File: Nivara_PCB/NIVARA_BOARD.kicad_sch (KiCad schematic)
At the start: 3 parts, among them U1 ESP32-S3-WROOM-1

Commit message: Cambios en la power supply.
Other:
- moved on the sheet: C1, R1, U1

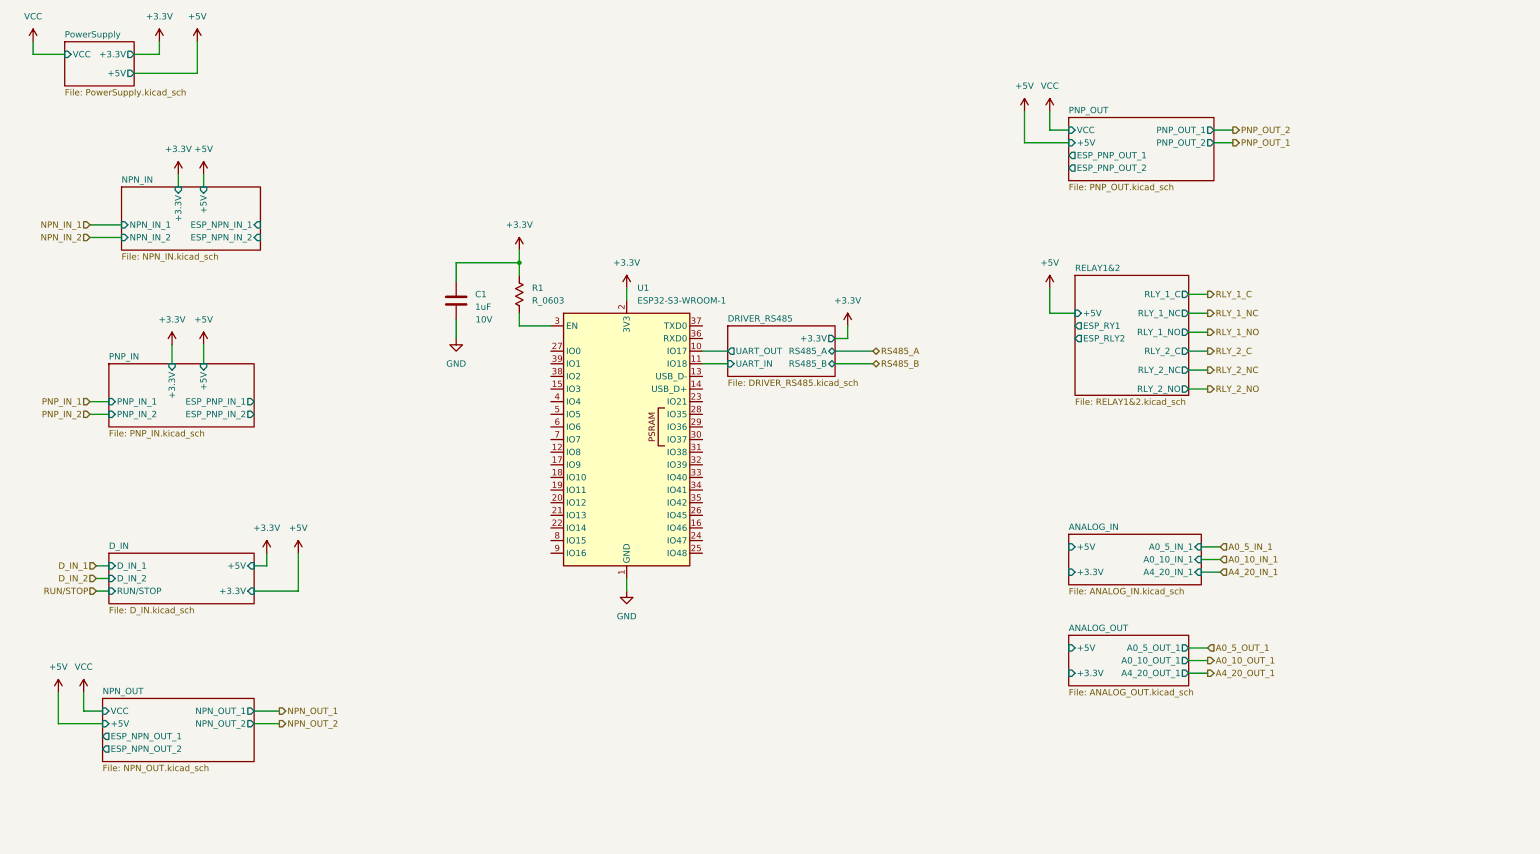
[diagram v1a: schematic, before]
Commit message: Cambios en las mediciones análogas.
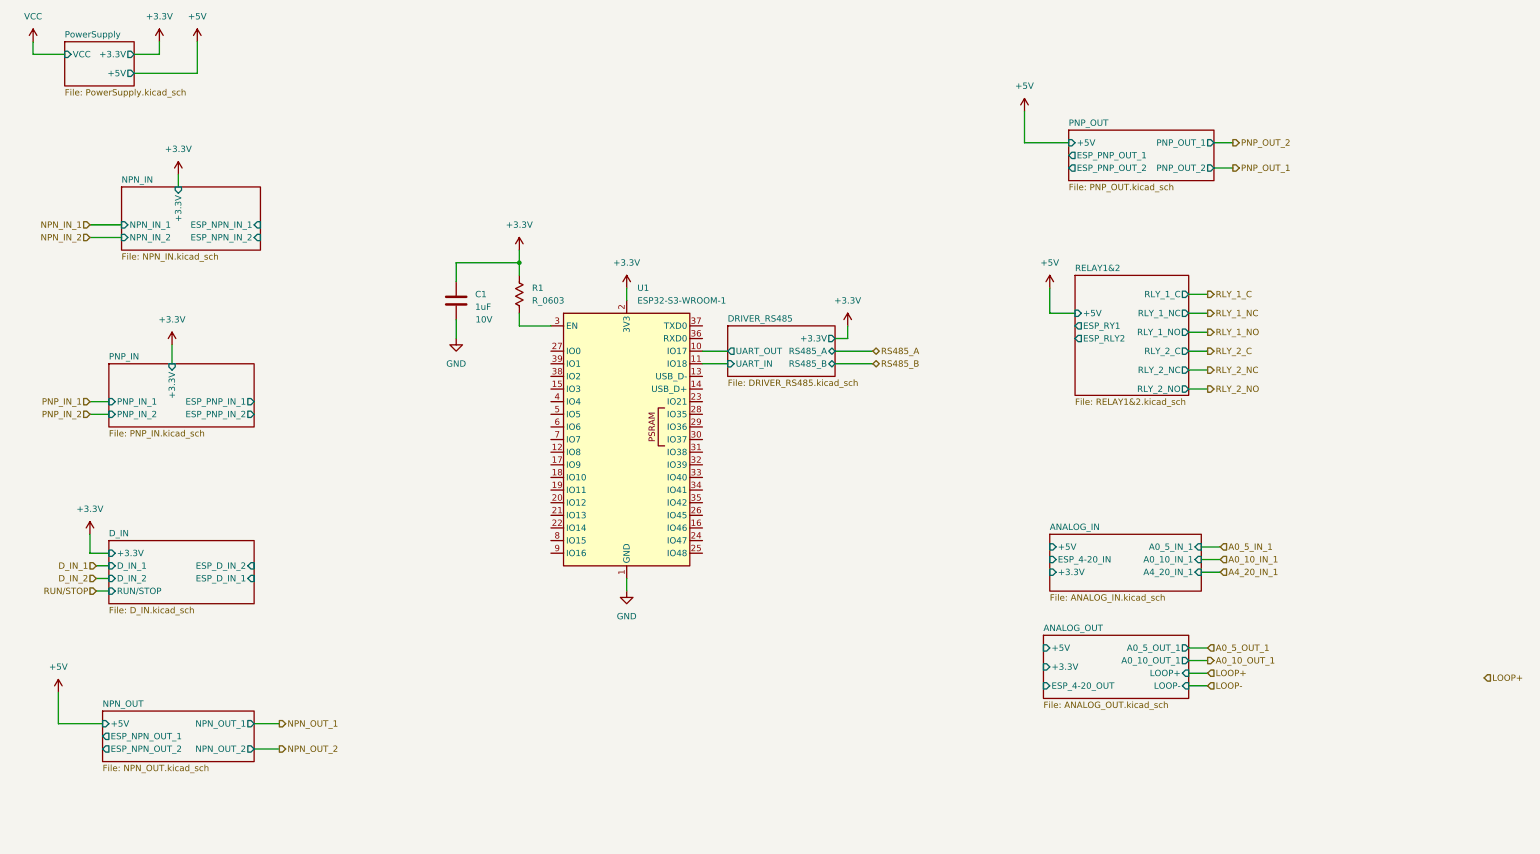
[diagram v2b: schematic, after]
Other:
- sheet ANALOG_IN ports: added ESP_4-20_IN; removed none
- sheet ANALOG_OUT ports: added ESP_4-20_OUT, LOOP+, LOOP-; removed A4_20_OUT_1
- sheet D_IN ports: added ESP_D_IN_1, ESP_D_IN_2; removed +5V
- sheet NPN_IN ports: added none; removed +5V
- sheet NPN_OUT ports: added none; removed VCC
- sheet PNP_IN ports: added none; removed +5V
- sheet PNP_OUT ports: added none; removed VCC

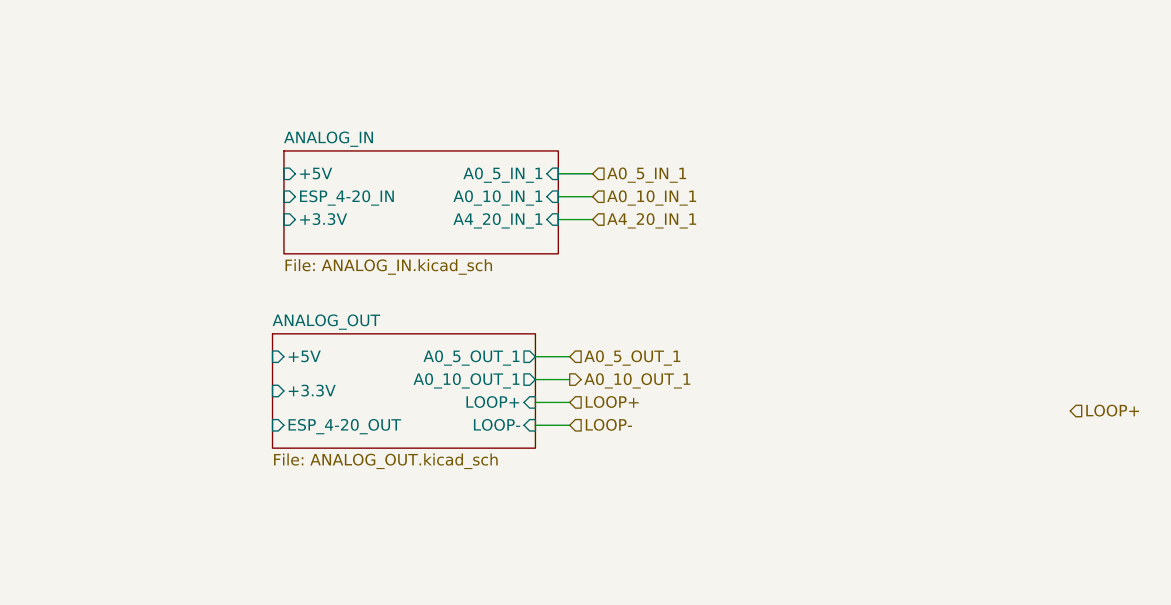
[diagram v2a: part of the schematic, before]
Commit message: Cambios en las salidas analogicas, ya que el ESP32 S3 no tiene DAC
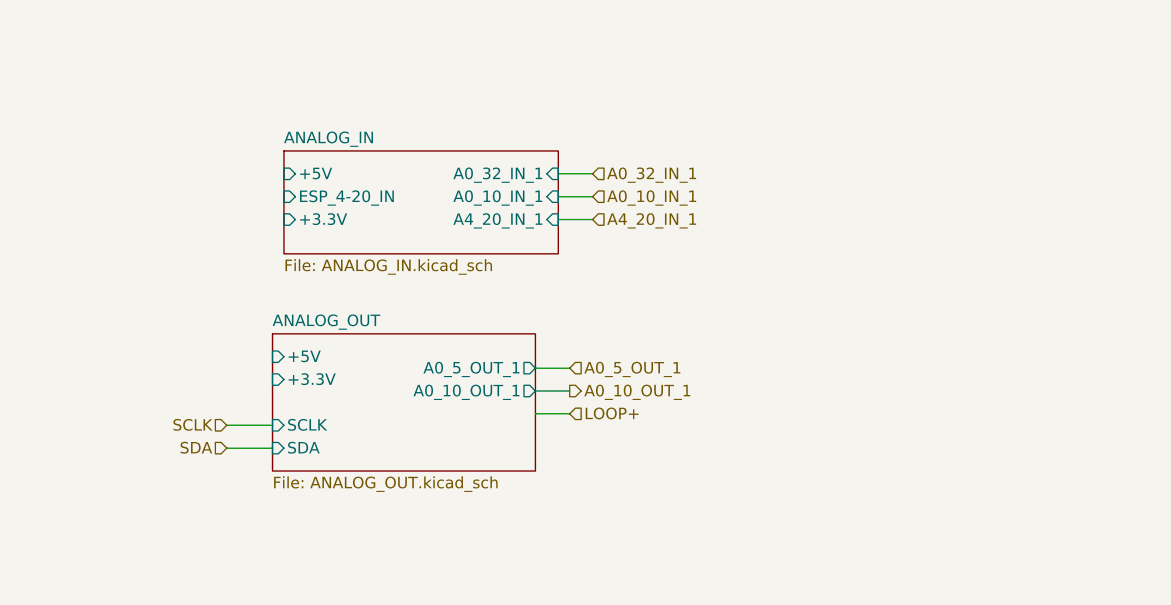
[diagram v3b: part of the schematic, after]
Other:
- sheet ANALOG_IN ports: added A0_32_IN_1; removed A0_5_IN_1
- sheet ANALOG_OUT ports: added SCLK, SDA; removed ESP_4-20_OUT, LOOP+, LOOP-
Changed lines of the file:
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@@
 	(wire
 		(pts
-			(xy 248.92 147.32) (xy 252.73 147.32)
+			(xy 248.92 148.59) (xy 252.73 148.59)
 		)
 		(stroke
@@
 	(wire
 		(pts
-			(xy 248.92 144.78) (xy 252.73 144.78)
+			(xy 248.92 146.05) (xy 252.73 146.05)
 		)
 		(stroke
@@
 	(wire
 		(pts
+			(xy 214.63 149.86) (xy 219.71 149.86)
+		)
+		(stroke
+			(width 0)
+			(type default)
+		)
+	)
+	(wire
+		(pts
 			(xy 215.9 40.64) (xy 224.79 40.64)
 		)
@@
 	(wire
 		(pts
-			(xy 248.92 142.24) (xy 252.73 142.24)
+			(xy 248.92 143.51) (xy 252.73 143.51)
 		)
 		(stroke
@@
 	(wire
 		(pts
+			(xy 214.63 152.4) (xy 219.71 152.4)
+		)
+		(stroke
+			(width 0)
+			(type default)
+		)
+	)
+	(wire
+		(pts
 			(xy 29.21 128.27) (xy 31.75 128.27)
 		)
@@
 		(pts
 			(xy 44.45 81.28) (xy 44.45 85.09)
-		)
-		(stroke
-			(width 0)
-			(type default)
-		)
-	)
-	(wire
-		(pts
-			(xy 248.92 149.86) (xy 252.73 149.86)
 		)
 		(stroke
@@
 	(hierarchical_label "A0_5_OUT_1"
 		(shape input)
-		(at 252.73 142.24 0)
+		(at 252.73 143.51 0)
 		(effects
 			(font
@@
 		)
 	)
+	(hierarchical_label "SCLK"
+		(shape input)
+		(at 214.63 149.86 180)
+		(effects
+			(font
+				(size 1.27 1.27)
+			)
+			(justify right)
+		)
+	)
 	(hierarchical_label "RLY_2_NO"
 		(shape output)
@@
 	(hierarchical_label "A0_10_OUT_1"
 		(shape output)
-		(at 252.73 144.78 0)
-		(effects
-			(font
-				(size 1.27 1.27)
-			)
-			(justify left)
-		)
-	)
-	(hierarchical_label "LOOP-"
-		(shape input)
-		(at 252.73 149.86 0)
+		(at 252.73 146.05 0)
 		(effects
 			(font
@@
 	(hierarchical_label "LOOP+"
 		(shape input)
-		(at 252.73 147.32 0)
+		(at 252.73 148.59 0)
 		(effects
 			(font
@@
 		)
 	)
-	(hierarchical_label "LOOP+"
+	(hierarchical_label "SDA"
 		(shape input)
-		(at 308.3444 148.2754 0)
+		(at 214.63 152.4 180)
 		(effects
 			(font
 				(size 1.27 1.27)
 			)
-			(justify left)
+			(justify right)
 		)
 	)
@@
 		)
 	)
-	(hierarchical_label "A0_5_IN_1"
+	(hierarchical_label "A0_32_IN_1"
 		(shape input)
 		(at 255.27 121.92 0)
@@
 			)
 		)
-		(pin "A0_5_IN_1" input
+		(pin "A0_32_IN_1" input
 			(at 251.46 121.92 0)
 			(effects
@@
 	(sheet
 		(at 219.71 139.7)
-		(size 29.21 12.7)
+		(size 29.21 15.24)
 		(exclude_from_sim no)
 		(in_bom yes)
@@
 		)
 		(property "Sheetfile" "ANALOG_OUT.kicad_sch"
-			(at 219.71 152.9846 0)
+			(at 219.71 155.5246 0)
 			(effects
 				(font
@@
 		)
 		(pin "+3.3V" input
-			(at 219.71 146.05 180)
+			(at 219.71 144.78 180)
 			(effects
 				(font
@@
 		)
 		(pin "A0_10_OUT_1" output
-			(at 248.92 144.78 0)
+			(at 248.92 146.05 0)
 			(effects
 				(font
@@
 		)
 		(pin "A0_5_OUT_1" output
-			(at 248.92 142.24 0)
+			(at 248.92 143.51 0)
 			(effects
 				(font
@@
 			)
 		)
-		(pin "ESP_4-20_OUT" input
+		(pin "SCLK" input
 			(at 219.71 149.86 180)
 			(effects
@@
 			)
 		)
-		(pin "LOOP+" input
-			(at 248.92 147.32 0)
-			(effects
-				(font
-					(size 1.27 1.27)
-				)
-				(justify right)
-			)
-		)
-		(pin "LOOP-" input
-			(at 248.92 149.86 0)
-			(effects
-				(font
-					(size 1.27 1.27)
-				)
-				(justify right)
-			)
-		)
+		(pin "SDA" input
+			(at 219.71 152.4 180)
+			(effects
+				(font
+					(size 1.27 1.27)
+				)
+				(justify left)
+			)
+		)

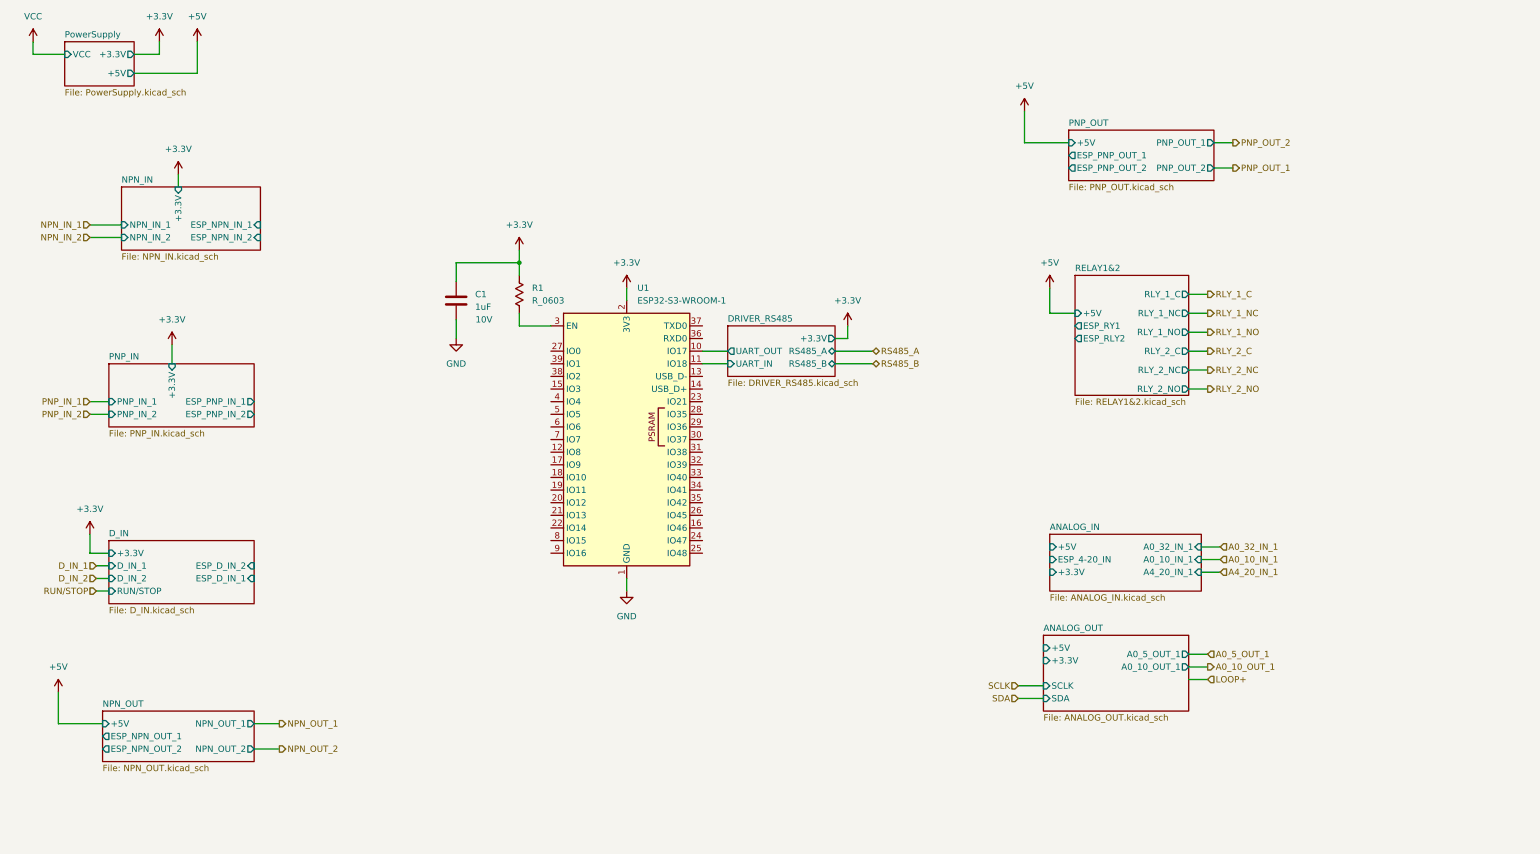
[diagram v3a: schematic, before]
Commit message: Cambios en los GPIO del ESP32
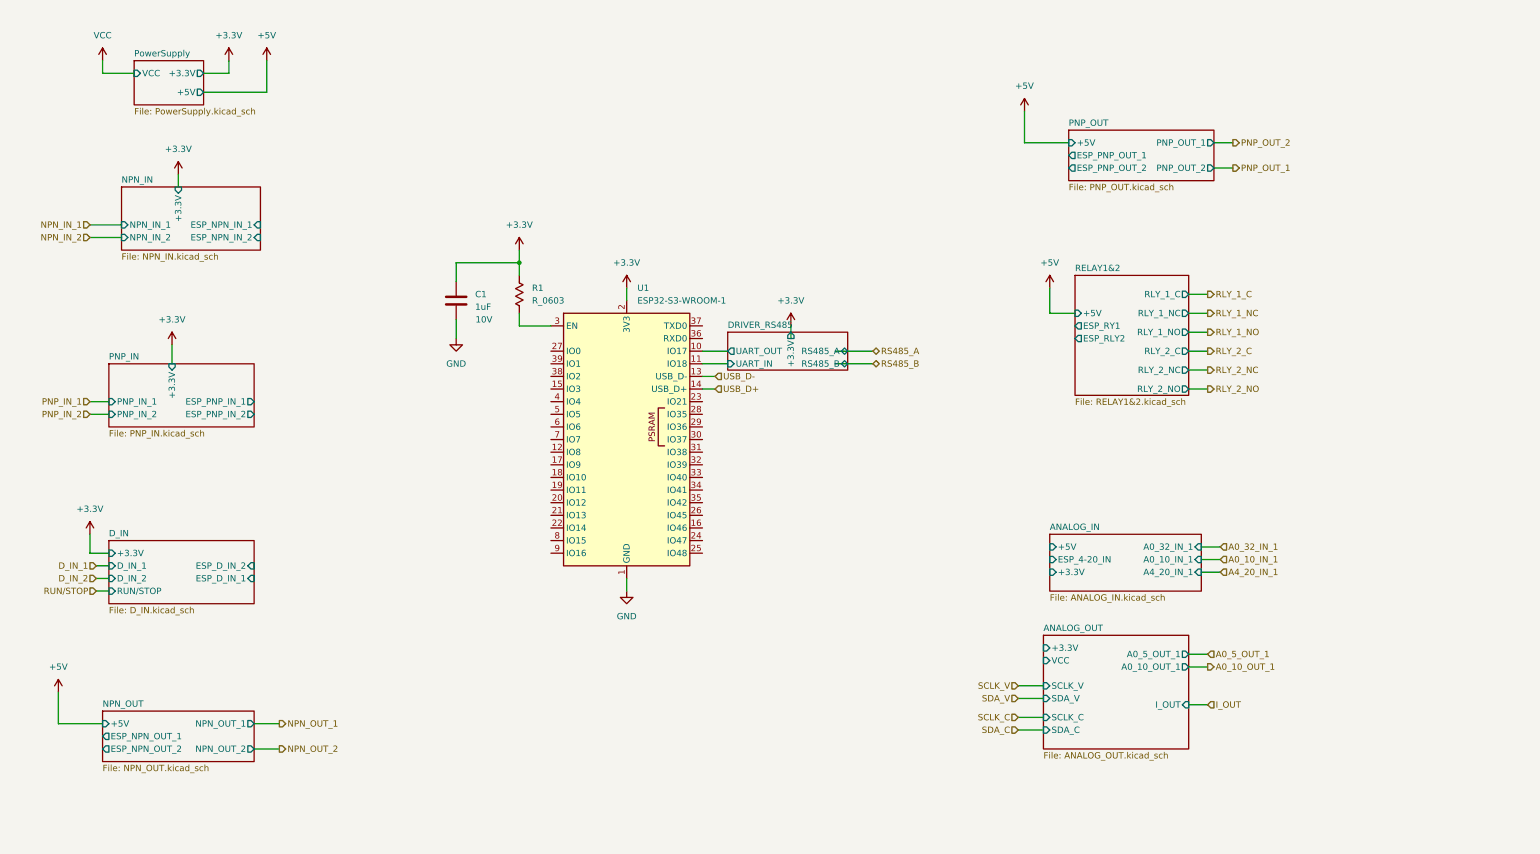
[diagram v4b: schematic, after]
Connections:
- net USB_D-: now reaches U1.13 (USB_D-)
- net USB_D+: now reaches U1.14 (USB_D+)
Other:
- sheet ANALOG_OUT ports: added I_OUT, SCLK_C, SCLK_V, SDA_C, SDA_V, VCC; removed +5V, SCLK, SDA

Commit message: Cambios en la medición de voltaje y corriente de la PCB Nivara.
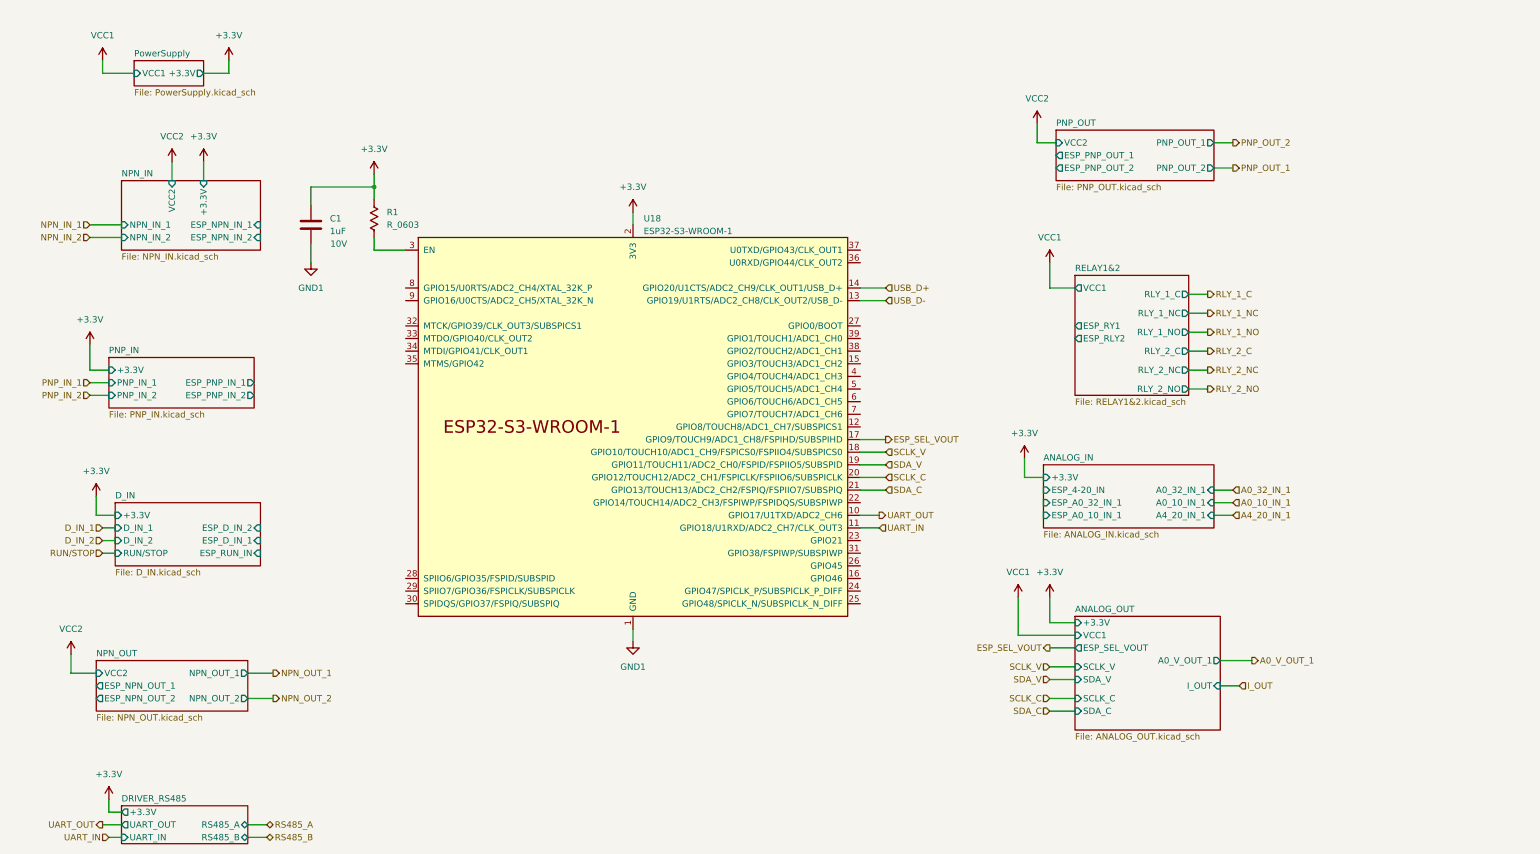
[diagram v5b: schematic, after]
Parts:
- removed U1: ESP32-S3-WROOM-1, RF_Module:ESP32-S3-WROOM-1, symbol RF_Module:ESP32-S3-WROOM-1
- added U18: ESP32-S3-WROOM-1, PCM_Espressif:ESP32-S3-WROOM-1, symbol PCM_Espressif:ESP32-S3-WROOM-1
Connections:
- net +3.3V: now also U18.2 (3V3)
- net SCLK_C: now also U18.20 (GPIO12/TOUCH12/ADC2_CH1/FSPICLK/FSPIIO6/SUBSPICLK)
- net SCLK_V: now also U18.18 (GPIO10/TOUCH10/ADC1_CH9/FSPICS0/FSPIIO4/SUBSPICS0)
- net SDA_C: now also U18.21 (GPIO13/TOUCH13/ADC2_CH2/FSPIQ/FSPIIO7/SUBSPIQ)
- net SDA_V: now also U18.19 (GPIO11/TOUCH11/ADC2_CH0/FSPID/FSPIIO5/SUBSPID)
- net USB_D+: now also U18.14 (GPIO20/U1CTS/ADC2_CH9/CLK_OUT1/USB_D+)
- net USB_D-: now also U18.13 (GPIO19/U1RTS/ADC2_CH8/CLK_OUT2/USB_D-)
- net at R1.2: now also U18.3 (EN)
- net GND renamed GND1
- net GND1: now also U18.1 (GND), U18.40 (GND), U18.41 (GND)
- new net ESP_SEL_VOUT: U18.17 (GPIO9/TOUCH9/ADC1_CH8/FSPIHD/SUBSPIHD)
- new net UART_IN: U18.11 (GPIO18/U1RXD/ADC2_CH7/CLK_OUT3)
- new net UART_OUT: U18.10 (GPIO17/U1TXD/ADC2_CH6)
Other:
- sheet ANALOG_IN ports: added ESP_A0_10_IN_1, ESP_A0_32_IN_1; removed +5V
- sheet ANALOG_OUT ports: added A0_V_OUT_1, ESP_SEL_VOUT, VCC1; removed A0_10_OUT_1, A0_5_OUT_1, VCC
- sheet D_IN ports: added ESP_RUN_IN; removed none
- sheet NPN_IN ports: added VCC2; removed none
- sheet NPN_OUT ports: added VCC2; removed +5V
- sheet PNP_OUT ports: added VCC2; removed +5V
- sheet PowerSupply ports: added VCC1; removed +5V, VCC
- sheet RELAY1&2 ports: added VCC1; removed +5V
- moved on the sheet: C1, R1
